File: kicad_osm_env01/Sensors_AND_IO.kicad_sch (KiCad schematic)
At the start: 41 parts, among them J1 STX-3000, J3 STX-3000, J4 DNF, J8 Conn_01x06, J9 STX-3000, U10 ICS-43434, U12 MIC94073YC6, U3 VEML7700-TT

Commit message: updated schematics
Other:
- sheet sheet60920843 ports: added none; removed PULSE1_PULLUP_EN, PULSE2_PULLUP_EN
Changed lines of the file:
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@@
     (stroke (width 0) (type default))
   )
-  (wire (pts (xy 39.37 178.435) (xy 48.895 178.435))
-    (stroke (width 0) (type default))
-  )
   (wire (pts (xy 354.965 95.25) (xy 354.965 92.71))
     (stroke (width 0) (type default))
@@
     (stroke (width 0) (type default))
   )
-  (wire (pts (xy 39.37 182.245) (xy 48.895 182.245))
-    (stroke (width 0) (type default))
-  )
   (wire (pts (xy 340.36 55.88) (xy 354.965 55.88))
     (stroke (width 0) (type default))
@@
     (effects (font (size 1.27 1.27)) (justify right bottom))
   )
-  (hierarchical_label "PULSE2_PULLUP_EN" (shape input) (at 39.37 182.245 180) (fields_autoplaced)
-    (effects (font (size 1.27 1.27)) (justify right))
-  )
   (hierarchical_label "HPM_EN" (shape input) (at 23.495 248.285 180) (fields_autoplaced)
     (effects (font (size 1.27 1.27)) (justify right))
@@
     (effects (font (size 1.27 1.27)) (justify right))
   )
-  (hierarchical_label "PULSE1_PULLUP_EN" (shape input) (at 39.37 178.435 180) (fields_autoplaced)
-    (effects (font (size 1.27 1.27)) (justify right))
-  )
   (hierarchical_label "PULSE_IN2" (shape input) (at 96.52 166.37 0) (fields_autoplaced)
     (effects (font (size 1.27 1.27)) (justify left))
@@
       (effects (font (size 1.27 1.27)) (justify right))
     )
-    (pin "PULSE2_PULLUP_EN" input (at 48.895 182.245 180)
-      (effects (font (size 1.27 1.27)) (justify left))
-    )
-    (pin "PULSE1_PULLUP_EN" input (at 48.895 178.435 180)
-      (effects (font (size 1.27 1.27)) (justify left))
-    )
     (pin "PULSE_IN2" input (at 84.455 166.37 0)

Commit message: added tracking to layout
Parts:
- TP13, TP14, TP48, TP49, TP56: footprint TestPoint:TestPoint_THTPad_D1.0mm_Drill0.5mm -> TestPoint:TestPoint_Pad_D1.5mm
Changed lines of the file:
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@@
       (effects (font (size 1.27 1.27)) hide)
     )
-    (property "Footprint" "TestPoint:TestPoint_THTPad_D1.0mm_Drill0.5mm" (at 96.52 227.965 0)
+    (property "Footprint" "TestPoint:TestPoint_Pad_D1.5mm" (at 96.52 227.965 0)
       (effects (font (size 1.27 1.27)) hide)
     )
@@
       (effects (font (size 1.27 1.27)) hide)
     )
-    (property "Footprint" "TestPoint:TestPoint_THTPad_D1.0mm_Drill0.5mm" (at 387.35 156.21 0)
+    (property "Footprint" "TestPoint:TestPoint_Pad_D1.5mm" (at 387.35 156.21 0)
       (effects (font (size 1.27 1.27)) hide)
     )
@@
       (effects (font (size 1.27 1.27)) hide)
     )
-    (property "Footprint" "TestPoint:TestPoint_THTPad_D1.0mm_Drill0.5mm" (at 198.755 90.805 0)
+    (property "Footprint" "TestPoint:TestPoint_Pad_D1.5mm" (at 198.755 90.805 0)
       (effects (font (size 1.27 1.27)) hide)
     )
@@
       (effects (font (size 1.27 1.27)) hide)
     )
-    (property "Footprint" "TestPoint:TestPoint_THTPad_D1.0mm_Drill0.5mm" (at 198.755 70.485 0)
+    (property "Footprint" "TestPoint:TestPoint_Pad_D1.5mm" (at 198.755 70.485 0)
       (effects (font (size 1.27 1.27)) hide)
     )
@@
       (effects (font (size 1.27 1.27)) hide)
     )
-    (property "Footprint" "TestPoint:TestPoint_THTPad_D1.0mm_Drill0.5mm" (at 238.125 77.47 0)
-      (effects (font (size 1.27 1.27)) hide)
-    )
+    (property "Footprint" "TestPoint:TestPoint_Pad_D1.5mm" (at 238.125 77.47 0)
+      (effects (font (size 1.27 1.27)) hide)
+    )

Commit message: minor updates to layout
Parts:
- removed J4: DNF, Devtank_PCB_lib:SEN54-SDN-T, symbol Connector_Generic:Conn_01x01
- added J4: Conn_01x06, Devtank_PCB_lib:SEN54-SDN-T, symbol Connector_Generic:Conn_01x06
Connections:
- no-connect marks 5 -> 10
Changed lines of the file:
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@@
   (junction (at 233.045 55.245) (diameter 0) (color 0 0 0 0)
   )
+  (no_connect (at 157.48 205.74))
   (no_connect (at 132.08 254))
-  (no_connect (at 154.305 197.485))
+  (no_connect (at 157.48 200.66))
   (no_connect (at 306.705 142.875))
+  (no_connect (at 157.48 195.58))
+  (no_connect (at 157.48 203.2))
   (no_connect (at 306.705 199.39))
+  (no_connect (at 157.48 208.28))
   (no_connect (at 306.705 176.53))
+  (no_connect (at 157.48 198.12))
   (wire (pts (xy 375.92 151.13) (xy 386.08 151.13))
     (stroke (width 0) (type default))
@@
     )
   )
+  (symbol (lib_id "Connector_Generic:Conn_01x06") (at 162.56 200.66 0) (unit 1)
+    (in_bom yes) (on_board yes) (dnp no) (fields_autoplaced)
+    (property "Reference" "J4" (at 164.592 200.906 0)
+      (effects (font (size 1.27 1.27)) (justify left))
+    )
+    (property "Value" "Conn_01x06" (at 164.592 202.954 0)
+      (effects (font (size 1.27 1.27)) (justify left))
+    )
+    (property "Footprint" "Devtank_PCB_lib:SEN54-SDN-T" (at 162.56 200.66 0)
+      (effects (font (size 1.27 1.27)) hide)
+    )
+    (property "Datasheet" "~" (at 162.56 200.66 0)
+      (effects (font (size 1.27 1.27)) hide)
+    )
+    (pin "1")
+    (pin "2")
+    (pin "3")
+    (pin "4")
+    (pin "5")
+    (pin "6")
+    (instances
+      (project "OSM_env01"
+        (path "/ab8b0540-9c9f-4195-88f5-7bed0b0a8ed6/00000000-0000-0000-0000-0000608f4675"
+          (reference "J4") (unit 1)
+        )
+      )
+    )
+  )
   (symbol (lib_id "Device:R") (at 323.215 201.93 0) (unit 1)
     (in_bom yes) (on_board yes) (dnp no)
@@
         )
       )
-    )
-  )
-  (symbol (lib_id "Connector_Generic:Conn_01x01") (at 159.385 197.485 0) (unit 1)
-    (in_bom yes) (on_board yes) (dnp no) (fields_autoplaced)
-    (property "Reference" "J4" (at 161.417 196.461 0)
-      (effects (font (size 1.27 1.27)) (justify left))
-    )
-    (property "Value" "DNF" (at 161.417 198.509 0)
-      (effects (font (size 1.27 1.27)) (justify left))
-    )
-    (property "Footprint" "Devtank_PCB_lib:SEN54-SDN-T" (at 159.385 197.485 0)
-      (effects (font (size 1.27 1.27)) hide)
-    )
-    (property "Datasheet" "~" (at 159.385 197.485 0)
-      (effects (font (size 1.27 1.27)) hide)
-    )
-    (pin "1")
-    (instances
-      (project "OSM_env01"
-        (path "/ab8b0540-9c9f-4195-88f5-7bed0b0a8ed6/00000000-0000-0000-0000-0000608f4675"
-          (reference "J4") (unit 1)
-        )
-      )

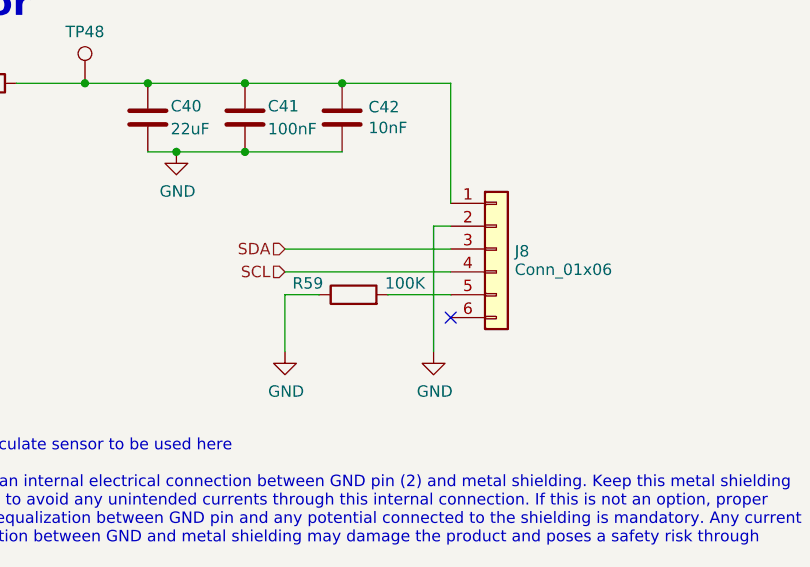
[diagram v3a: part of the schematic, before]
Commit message: updated stm32 pinmap
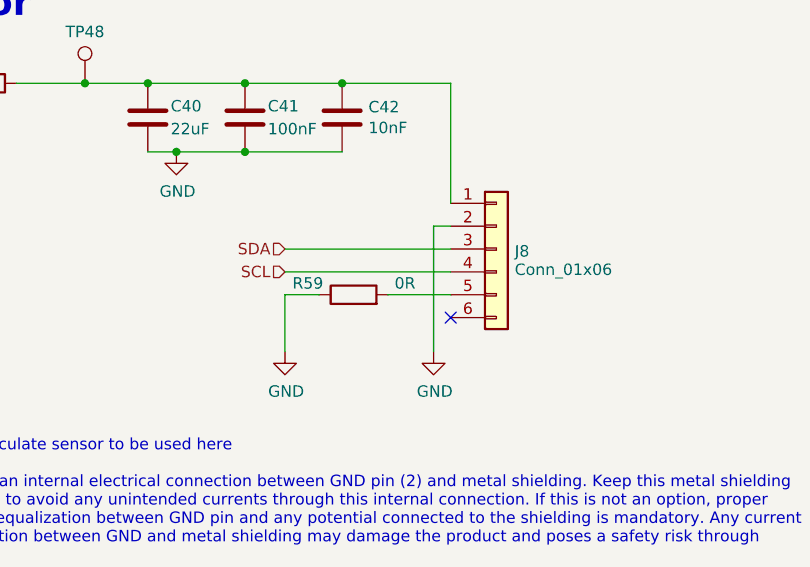
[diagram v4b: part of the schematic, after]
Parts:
- R59: value 100K -> 0R
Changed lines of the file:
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@@
       (effects (font (size 1.27 1.27)))
     )
-    (property "Value" "100K" (at 127 250.19 90)
+    (property "Value" "0R" (at 127 250.19 90)
       (effects (font (size 1.27 1.27)))
     )

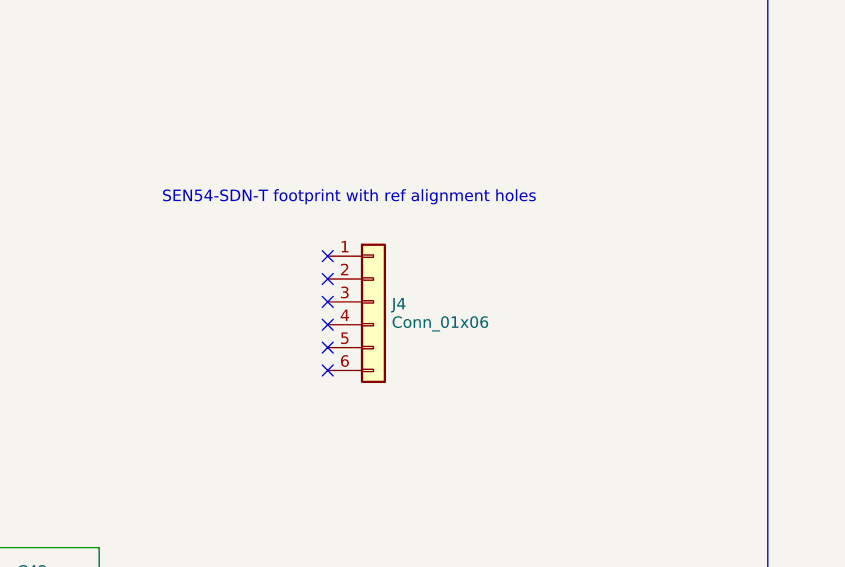
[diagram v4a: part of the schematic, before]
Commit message: d sub pinmap change to suport RS485 or CAN
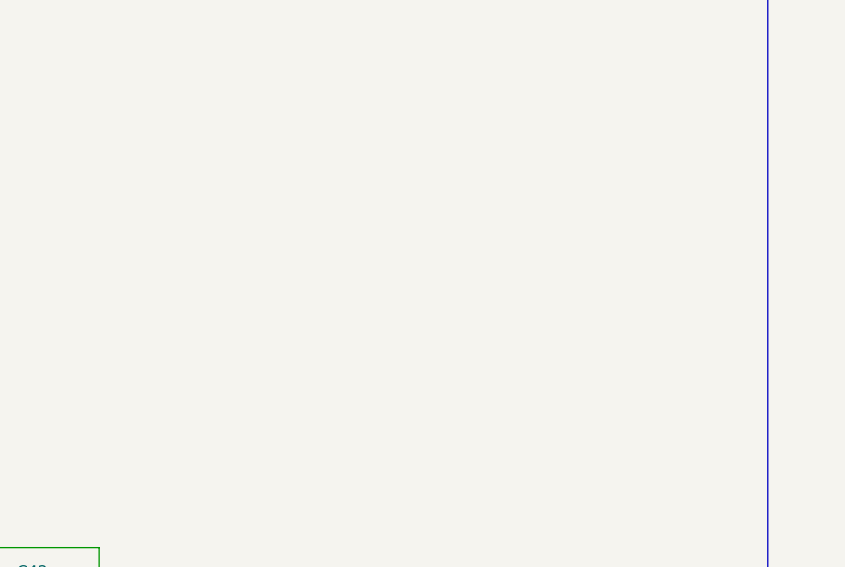
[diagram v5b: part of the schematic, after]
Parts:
- removed J4: Conn_01x06, Devtank_PCB_lib:SEN54-SDN-T, symbol Connector_Generic:Conn_01x06
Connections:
- no-connect marks 10 -> 4
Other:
- note removed: "SEN54-SDN-T footprint with ref alignment holes"
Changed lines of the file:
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@@
   (junction (at 233.045 55.245) (diameter 0) (color 0 0 0 0)
   )
-  (no_connect (at 157.48 205.74))
   (no_connect (at 132.08 254))
-  (no_connect (at 157.48 200.66))
   (no_connect (at 306.705 142.875))
-  (no_connect (at 157.48 195.58))
-  (no_connect (at 157.48 203.2))
   (no_connect (at 306.705 199.39))
-  (no_connect (at 157.48 208.28))
   (no_connect (at 306.705 176.53))
-  (no_connect (at 157.48 198.12))
   (wire (pts (xy 375.92 151.13) (xy 386.08 151.13))
     (stroke (width 0) (type default))
@@
     (effects (font (size 2.9972 2.9972) (thickness 0.5994) bold) (justify left bottom))
   )
-  (text "SEN54-SDN-T footprint with ref alignment holes" (at 139.065 189.865 0)
-    (effects (font (size 1.27 1.27)) (justify left bottom))
-  )
   (text "CT Clamp 1\n\n" (at 230.505 153.035 0)
     (effects (font (size 2.9972 2.9972) (thickness 0.5994) bold) (justify left bottom))
@@
         )
       )
-    )
-  )
-  (symbol (lib_id "Connector_Generic:Conn_01x06") (at 162.56 200.66 0) (unit 1)
-    (in_bom yes) (on_board yes) (dnp no) (fields_autoplaced)
-    (property "Reference" "J4" (at 164.592 200.906 0)
-      (effects (font (size 1.27 1.27)) (justify left))
-    )
-    (property "Value" "Conn_01x06" (at 164.592 202.954 0)
-      (effects (font (size 1.27 1.27)) (justify left))
-    )
-    (property "Footprint" "Devtank_PCB_lib:SEN54-SDN-T" (at 162.56 200.66 0)
-      (effects (font (size 1.27 1.27)) hide)
-    )
-    (property "Datasheet" "~" (at 162.56 200.66 0)
-      (effects (font (size 1.27 1.27)) hide)
-    )
-    (pin "1")
-    (pin "2")
-    (pin "3")
-    (pin "4")
-    (pin "5")
-    (pin "6")
-    (instances
-      (project "OSM_env01"
-        (path "/ab8b0540-9c9f-4195-88f5-7bed0b0a8ed6/00000000-0000-0000-0000-0000608f4675"
-          (reference "J4") (unit 1)
-        )
-      )

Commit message: layout updated with a few ic packages due to errors, silk screen tidy up, logos added, minor update to rs232 schematics and pinmap to stm
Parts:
- U10: footprint Devtank_PCB_lib:ICS-43434 -> Devtank_PCB_lib:ICS-43434_kicad_v7
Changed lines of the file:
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@@
       (effects (font (size 1.27 1.27)))
     )
-    (property "Footprint" "Devtank_PCB_lib:ICS-43434" (at 215.265 76.835 0)
+    (property "Footprint" "Devtank_PCB_lib:ICS-43434_kicad_v7" (at 215.265 76.835 0)
       (effects (font (size 1.27 1.27)) (justify left bottom) hide)
     )

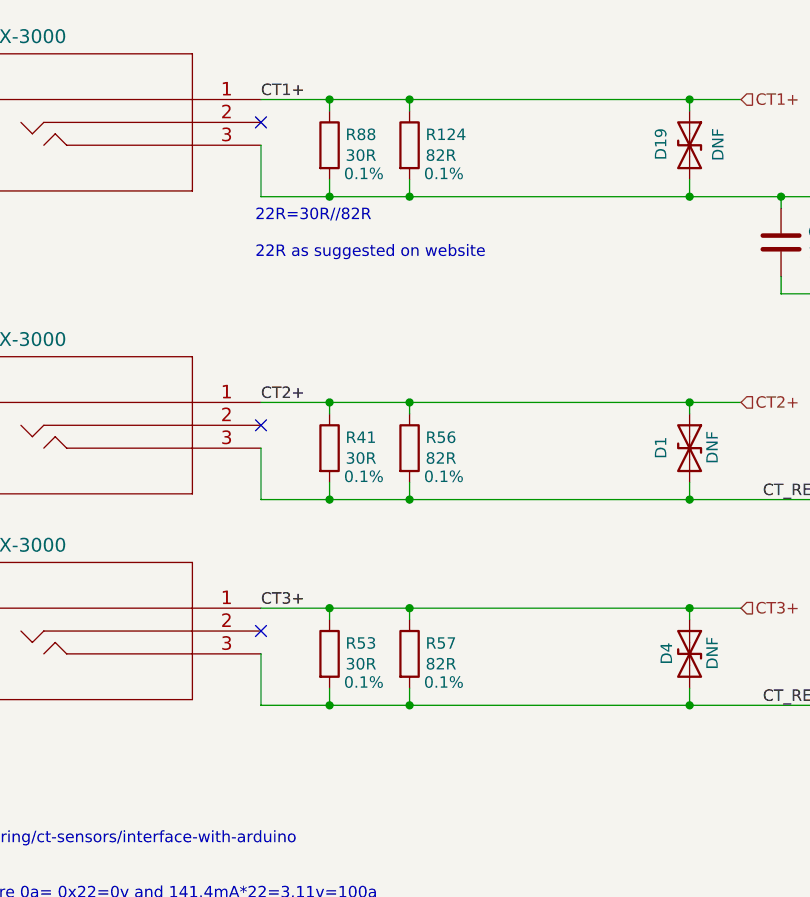
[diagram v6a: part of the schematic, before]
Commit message: added information to symbol entries table, added jumper settings table, minor single track update on layout
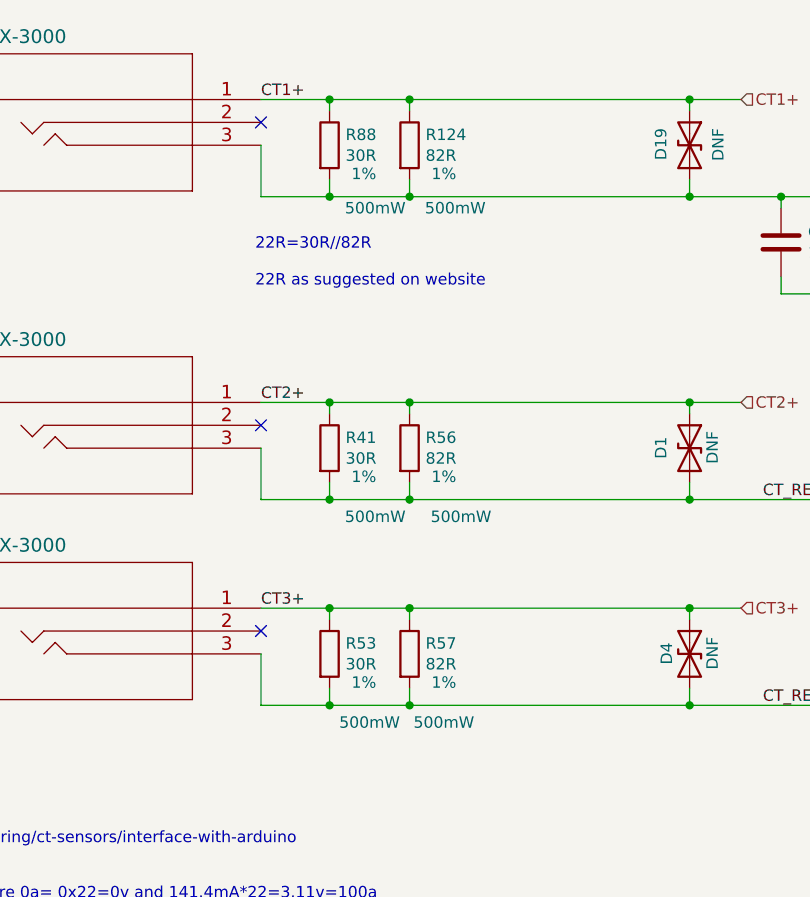
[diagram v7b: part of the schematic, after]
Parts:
- C39, C4, C41, C56, C71: Characteristics (none) -> X5R; Other (none) -> Can use own part, but needs to meet the specs
- C40, C42, C69: Characteristics (none) -> X5R; Other (none) -> Can use own part, but needs to meet the specs; Voltage (none) -> 10V
- C55: Characteristics (none) -> X5R; Voltage (none) -> 50V
- J1, J3, J9: Manufacturer (none) -> Kycon; Manufacturer Part Number (none) -> STX-3000
- J8: Manufacturer (none) -> JST; Manufacturer Part Number (none) -> BM06B-GHS-TBT
- L12, L3: Manufacturer (none) -> TDK; Manufacturer Part Number (none) -> MPZ1005S121HT000; Other (none) -> Can use own part, but needs to meet the specs
- R124, R56, R57: Manufacturer (none) -> Muticomp; Manufacturer Part Number (none) -> MCHP06W2F820JT5E; Other (none) -> Can use own part, but needs to meet the specs; Power Rating (none) -> 500mW; Tolerance 0.1% -> 1%
- R39, R40, R59, R96, R97, R99: Tolerance (none) -> 1%
- R41, R53, R88: Manufacturer (none) -> YAGEO; Manufacturer Part Number (none) -> RC1206FR-7W30RL; Other (none) -> Can use own part, but needs to meet the specs; Power Rating (none) -> 500mW; Tolerance 0.1% -> 1%
- U10: Manufacturer (none) -> TDK InvenSense; Manufacturer Part Number (none) -> ICS-43434
- U12: Manufacturer (none) -> Microchip Technology; Manufacturer Part Number (none) -> MIC94073YC6-TR
- U3: Manufacturer (none) -> VISHAY; Manufacturer Part Number (none) -> VEML7700-TT
